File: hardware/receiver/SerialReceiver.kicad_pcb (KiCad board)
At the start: 2 copper layers, 78.7 x 70.5 mm, 30 parts, among them J1 DATA, J2 CONTROL, J3 RX, J4 Clock select, J5 Conn_01x03_Male, J6 Clock select, SW1 SW_Push, U1 74HC132, U2 74HC191, U3 74HC191, U4 74HC595, U5 74HC74, U6 74LS244

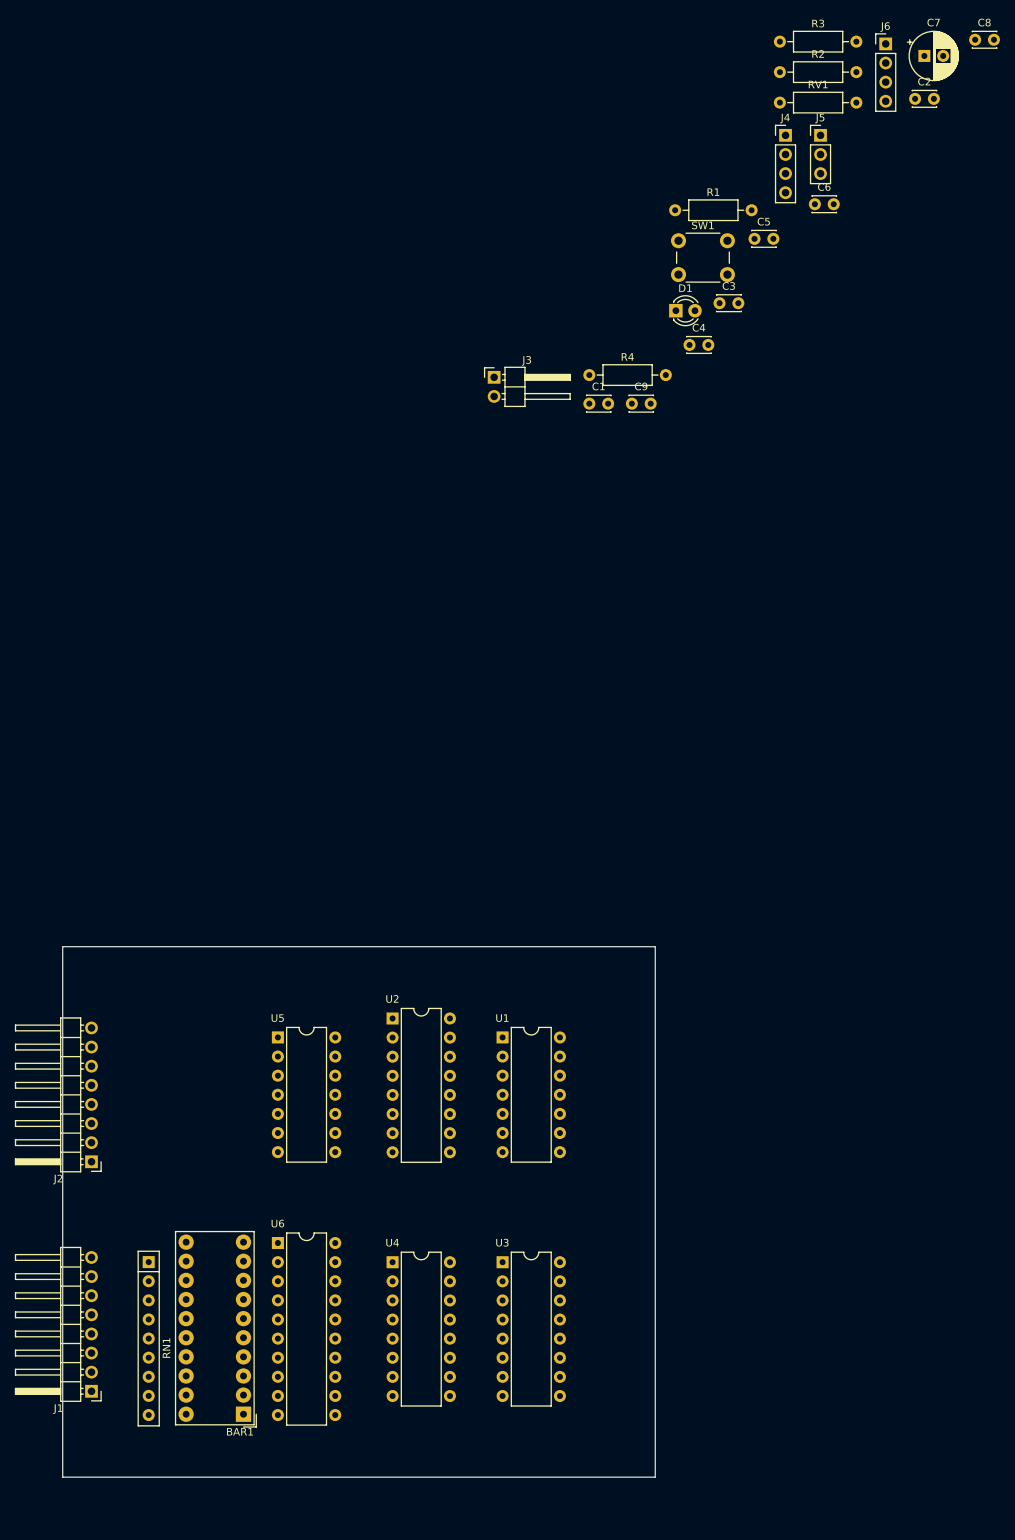
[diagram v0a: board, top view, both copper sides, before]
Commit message: Changed the layout of the schematic for better wiring.
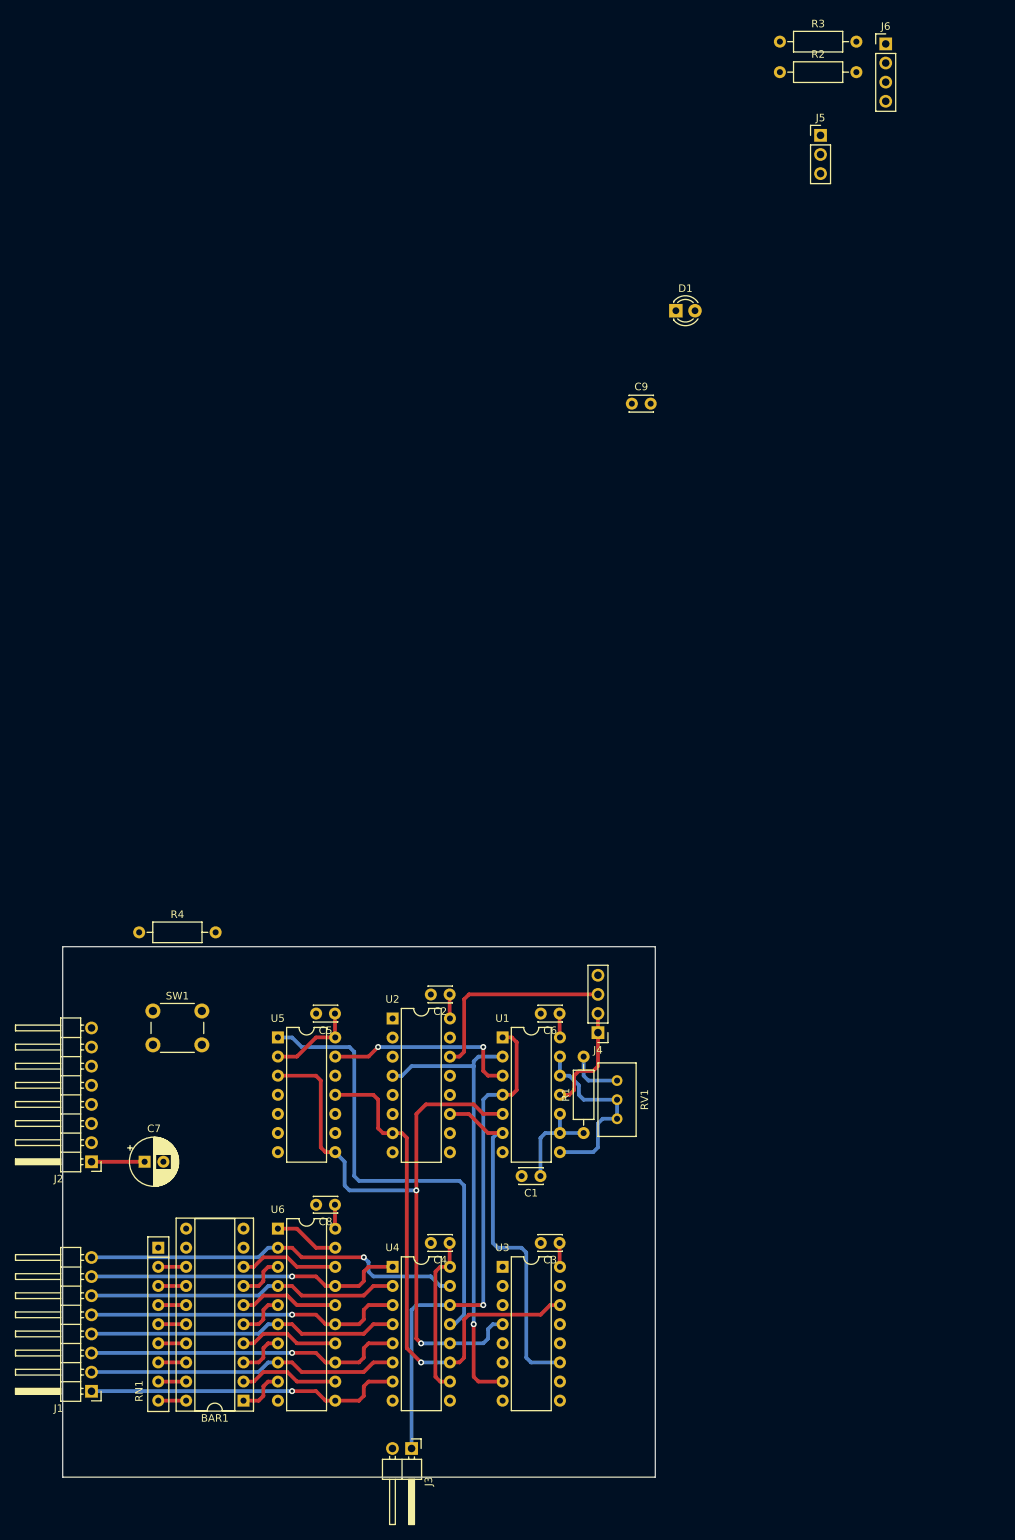
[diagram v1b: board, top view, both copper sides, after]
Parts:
- BAR1: footprint Display:HDSP-4830 -> Package_DIP:DIP-20_W7.62mm_Socket
- RV1: footprint Resistor_THT:R_Axial_DIN0207_L6.3mm_D2.5mm_P10.16mm_Horizontal -> Potentiometer_THT:Potentiometer_Bourns_3296W_Vertical
- moved C7 179.8 mm to (130.3, 90.8)
- moved C8 176.6 mm to (155.6, 96.5), turned to 180 degrees
- moved J3 142.7 mm to (165.7, 128.9), turned to -90 degrees
- moved RV1 136.7 mm to (193.0, 85.1), turned to -90 degrees
- moved C2 134.1 mm to (170.8, 68.6), turned to 180 degrees
- moved C3 126.7 mm to (185.4, 101.6), turned to 180 degrees
- moved SW1 123.9 mm to (131.4, 70.8)
- moved C4 123.5 mm to (170.8, 101.6), turned to 180 degrees
- moved R1 123.2 mm to (188.6, 87.0), turned to 90 degrees
- moved J4 121.8 mm to (190.5, 73.7), turned to 180 degrees
- moved C5 117.1 mm to (155.6, 71.1), turned to 180 degrees
- moved C6 112.8 mm to (185.4, 71.1), turned to 180 degrees
- moved C1 102.8 mm to (182.9, 92.7), turned to 180 degrees
- moved R4 95.2 mm to (129.5, 60.3)
- moved RN1 2.29 mm to (132.1, 102.2)
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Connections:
- BAR1 pad 1: Net-(BAR1-Pad1) -> /DO0
- BAR1 pad 2: Net-(BAR1-Pad2) -> /DO1
- BAR1 pad 3: Net-(BAR1-Pad3) -> /DO2
- BAR1 pad 4: Net-(BAR1-Pad4) -> /DO3
- BAR1 pad 5: Net-(BAR1-Pad5) -> /DO4
- BAR1 pad 6: Net-(BAR1-Pad6) -> /DO5
- BAR1 pad 7: Net-(BAR1-Pad7) -> /DO6
- BAR1 pad 8: Net-(BAR1-Pad8) -> /DO7
- RN1 pad 2: Net-(BAR1-Pad20) -> Net-(BAR1-Pad13)
- RN1 pad 3: Net-(BAR1-Pad19) -> Net-(BAR1-Pad14)
- RN1 pad 4: Net-(BAR1-Pad18) -> Net-(BAR1-Pad15)
- RN1 pad 5: Net-(BAR1-Pad17) -> Net-(BAR1-Pad16)
- RN1 pad 6: Net-(BAR1-Pad16) -> Net-(BAR1-Pad17)
- RN1 pad 7: Net-(BAR1-Pad15) -> Net-(BAR1-Pad18)
- RN1 pad 8: Net-(BAR1-Pad14) -> Net-(BAR1-Pad19)
- RN1 pad 9: Net-(BAR1-Pad13) -> Net-(BAR1-Pad20)
- U1 pad 1: Net-(C1-Pad1) -> Net-(J3-Pad1)
- U1 pad 10: Net-(U1-Pad10) -> Net-(C1-Pad1)
- U1 pad 11: Net-(U1-Pad11) -> Net-(J4-Pad1)
- U1 pad 12: Net-(J3-Pad1) -> Net-(RV1-Pad1)
- U1 pad 13: Net-(U1-Pad13) -> Net-(RV1-Pad1)
- U1 pad 2: Net-(C1-Pad1) -> Net-(U2-Pad4)
- U1 pad 3: Net-(RV1-Pad1) -> Net-(U5-Pad13)
- U1 pad 4: Net-(RV1-Pad1) -> Net-(J3-Pad1)
- U1 pad 5: Net-(RV1-Pad1) -> Net-(U3-Pad4)
- U1 pad 6: Net-(J4-Pad1) -> Net-(U2-Pad11)
- U1 pad 8: Net-(U1-Pad8) -> Net-(RV1-Pad1)
- U1 pad 9: Net-(J3-Pad1) -> Net-(C1-Pad1)
- U2 pad 11: Net-(U1-Pad8) -> Net-(U2-Pad11)
- U2 pad 4: Net-(U1-Pad13) -> Net-(U2-Pad4)
- U3 pad 11: Net-(U1-Pad8) -> Net-(U2-Pad11)
- U3 pad 4: Net-(U1-Pad10) -> Net-(U3-Pad4)
- U3 pad 7: Net-(U1-Pad13) -> Net-(U2-Pad4)
- U4 pad 1: /D1 -> /D6
- U4 pad 12: Net-(U1-Pad10) -> Net-(U3-Pad4)
- U4 pad 15: /D0 -> /D7
- U4 pad 2: /D2 -> /D5
- U4 pad 3: /D3 -> /D4
- U4 pad 4: /D4 -> /D3
- U4 pad 5: /D5 -> /D2
- U4 pad 6: /D6 -> /D1
- U4 pad 7: /D7 -> /D0
- U5 pad 1: Net-(U1-Pad11) -> Net-(J2-Pad4)
- U5 pad 11: Net-(U1-Pad10) -> Net-(U2-Pad7)
- U5 pad 13: Net-(J2-Pad4) -> Net-(U5-Pad13)
- U5 pad 3: Net-(U2-Pad7) -> Net-(U3-Pad4)
- U5 pad 5: unconnected-(U5-Pad5) -> Net-(J2-Pad7)
- U5 pad 6: Net-(U1-Pad10) -> Net-(D1-Pad1)
- U5 pad 8: Net-(D1-Pad1) -> Net-(U3-Pad4)
- U5 pad 9: Net-(J2-Pad7) -> unconnected-(U5-Pad9)
- U6 pad 11: /D7 -> /D0
- U6 pad 12: Net-(BAR1-Pad4) -> /DO1
- U6 pad 13: /D5 -> /D2
- U6 pad 14: Net-(BAR1-Pad3) -> /DO3
- U6 pad 15: /D3 -> /D4
- U6 pad 16: Net-(BAR1-Pad2) -> /DO5
- U6 pad 17: /D1 -> /D6
- U6 pad 18: Net-(BAR1-Pad1) -> /DO7
- U6 pad 2: /D0 -> /D7
- U6 pad 3: Net-(BAR1-Pad8) -> /DO6
- U6 pad 4: /D2 -> /D5
- U6 pad 5: Net-(BAR1-Pad7) -> /DO4
- U6 pad 6: /D4 -> /D3
- U6 pad 7: Net-(BAR1-Pad6) -> /DO2
- U6 pad 8: /D6 -> /D1
- U6 pad 9: Net-(BAR1-Pad5) -> /DO0
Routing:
- net Net-(U3-Pad4): track 0.00 -> 87.7 mm, vias 0 -> 2
- net Net-(U2-Pad7): track 0.00 -> 69.3 mm, vias 0 -> 1
- net Net-(J3-Pad1): track 0.00 -> 69.0 mm, vias 0 -> 1
- net Net-(J2-Pad4): track 0.00 -> 62.1 mm
- net Net-(U2-Pad4): track 0.00 -> 61.4 mm, vias 0 -> 1
- net VCC: track 0.00 -> 53.2 mm
- net /D7: track 0.00 -> 51.0 mm, vias 0 -> 1
- net Net-(U2-Pad11): track 0.00 -> 47.3 mm
- net /D0: track 0.00 -> 42.3 mm, vias 0 -> 1
- net /D6: track 0.00 -> 42.3 mm, vias 0 -> 1
- net /D4: track 0.00 -> 42.3 mm, vias 0 -> 1
- net /D2: track 0.00 -> 42.3 mm, vias 0 -> 1
- net /D3: track 0.00 -> 41.6 mm
- net /D1: track 0.00 -> 41.6 mm
- net /D5: track 0.00 -> 41.6 mm
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
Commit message: Made an RX input protection, and almost finished the PCB.
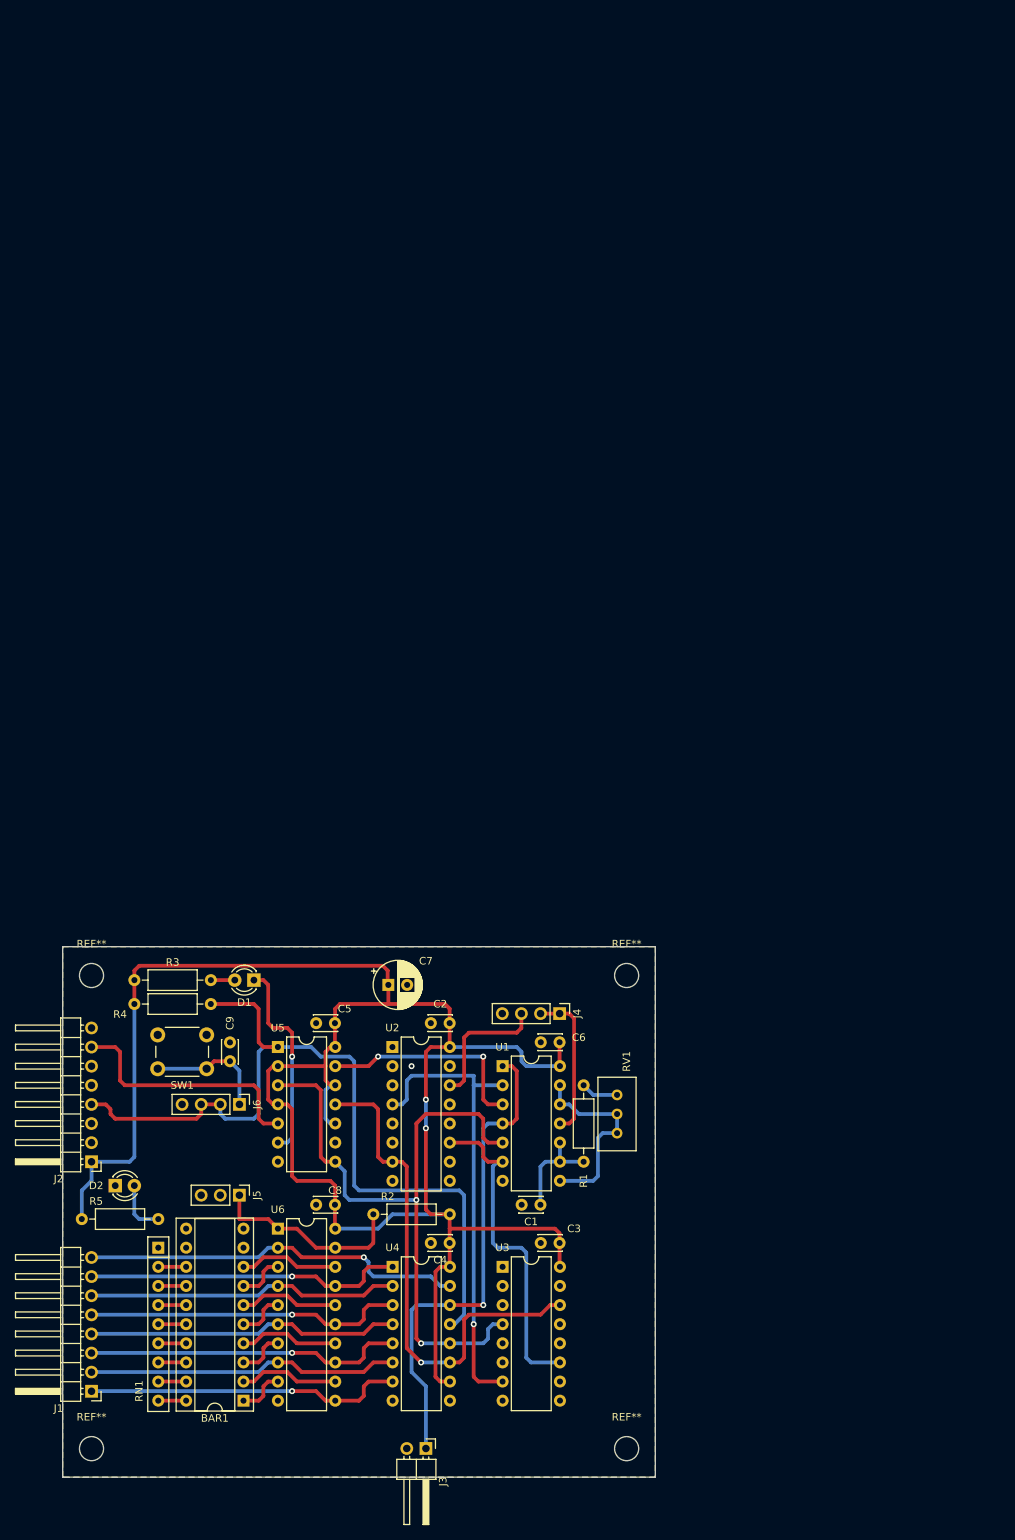
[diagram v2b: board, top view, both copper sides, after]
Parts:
- added D2: LED, LED_THT:LED_D3.0mm, F.Cu at (126.4, 94.0)
- added R5: 1k, Resistor_THT:R_Axial_DIN0207_L6.3mm_D2.5mm_P10.16mm_Horizontal, F.Cu at (121.9, 98.4)
- added REF**: MountingHole_3.2mm_M3, MountingHole:MountingHole_3.2mm_M3, F.Cu at (194.3, 66.1)
- added REF**: MountingHole_3.2mm_M3, MountingHole:MountingHole_3.2mm_M3, F.Cu at (123.2, 66.1)
- added REF**: MountingHole_3.2mm_M3, MountingHole:MountingHole_3.2mm_M3, F.Cu at (123.2, 128.9)
- added REF**: MountingHole_3.2mm_M3, MountingHole:MountingHole_3.2mm_M3, F.Cu at (194.3, 128.9)
- J5: value Conn_01x03_Male -> LED enable
- J6: value Clock select -> Mode select
- moved J6 165.0 mm to (142.9, 83.2), turned to -90 degrees
- moved R2 161.1 mm to (160.7, 97.8)
- moved J5 160.6 mm to (142.9, 95.2), turned to -90 degrees
- moved R3 151.3 mm to (128.9, 66.7)
- moved D1 105.1 mm to (144.8, 66.7), turned to 180 degrees
- moved C9 102.4 mm to (141.6, 77.5), turned to 90 degrees
- moved C7 40.0 mm to (162.6, 67.3)
- moved R4 13.5 mm to (139.1, 69.8), turned to 180 degrees
- moved J4 5.68 mm to (185.4, 71.1), turned to -90 degrees
- moved C1 3.81 mm to (182.9, 96.5)
- moved C2 3.81 mm to (170.8, 72.4)
- moved C6 3.81 mm to (185.4, 74.9)
- moved R1 3.81 mm to (188.6, 90.8)
- moved U1 3.81 mm to (177.8, 78.1)
- moved U2 3.80 mm to (163.2, 75.6)
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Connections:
- R4 pad 1: Net-(C9-Pad1) -> Net-(J2-Pad4)
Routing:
- net VCC: track 53.2 -> 261.8 mm, vias 0 -> 1
- net Net-(J2-Pad4): track 62.1 -> 112.5 mm
- net Net-(J2-Pad7): track 0.00 -> 33.4 mm
- net Net-(D1-Pad1): track 0.00 -> 27.1 mm, vias 0 -> 1
- net Net-(J5-Pad1): track 8.68 -> 26.6 mm
- net Net-(C9-Pad1): track 0.00 -> 16.3 mm
- net Net-(J4-Pad3): track 27.2 -> 17.9 mm
- net Net-(D2-Pad2): track 0.00 -> 7.25 mm
- net Net-(J4-Pad1): track 14.7 -> 20.2 mm
- net Net-(D1-Pad2): track 0.00 -> 3.18 mm
- net Net-(U1-Pad6): track 47.3 -> 44.2 mm
- net Net-(J3-Pad1): track 69.0 -> 66.0 mm
- net Net-(U1-Pad3): track 26.2 -> 28.7 mm
- net Net-(R1-Pad2): track 7.25 -> 4.98 mm
- net Net-(U2-Pad7): track 69.3 -> 68.1 mm
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- added copper zone on B.Cu, net GND
- added copper zone on F.Cu, net GND
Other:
- board text added: "!RD"
- board text added: "ALWAYS"
- board text added: "BUTTON"
- board text added: "D0"
- board text added: "D1"
- board text added: "D2"
- board text added: "D3"
- board text added: "D4"
- board text added: "D5"
- board text added: "D6"
- board text added: "D7"
- board text added: "EXT. CLOCK"
- board text added: "GND"
- board text added: "MANUAL"
- board text added: "ON"
- board text added: "READY"
- board text added: "Ready"
- board text added: "VCC"

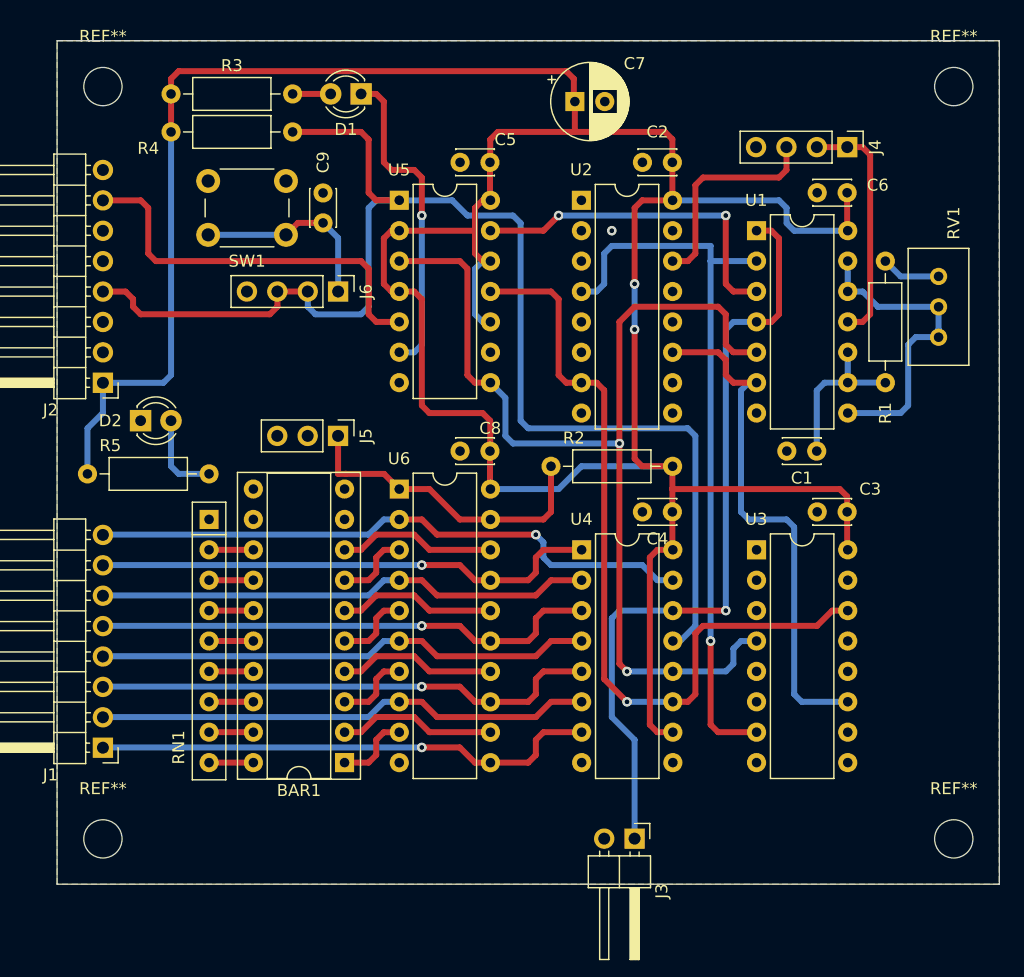
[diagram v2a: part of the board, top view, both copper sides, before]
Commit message: Input protection is now on the PCB.
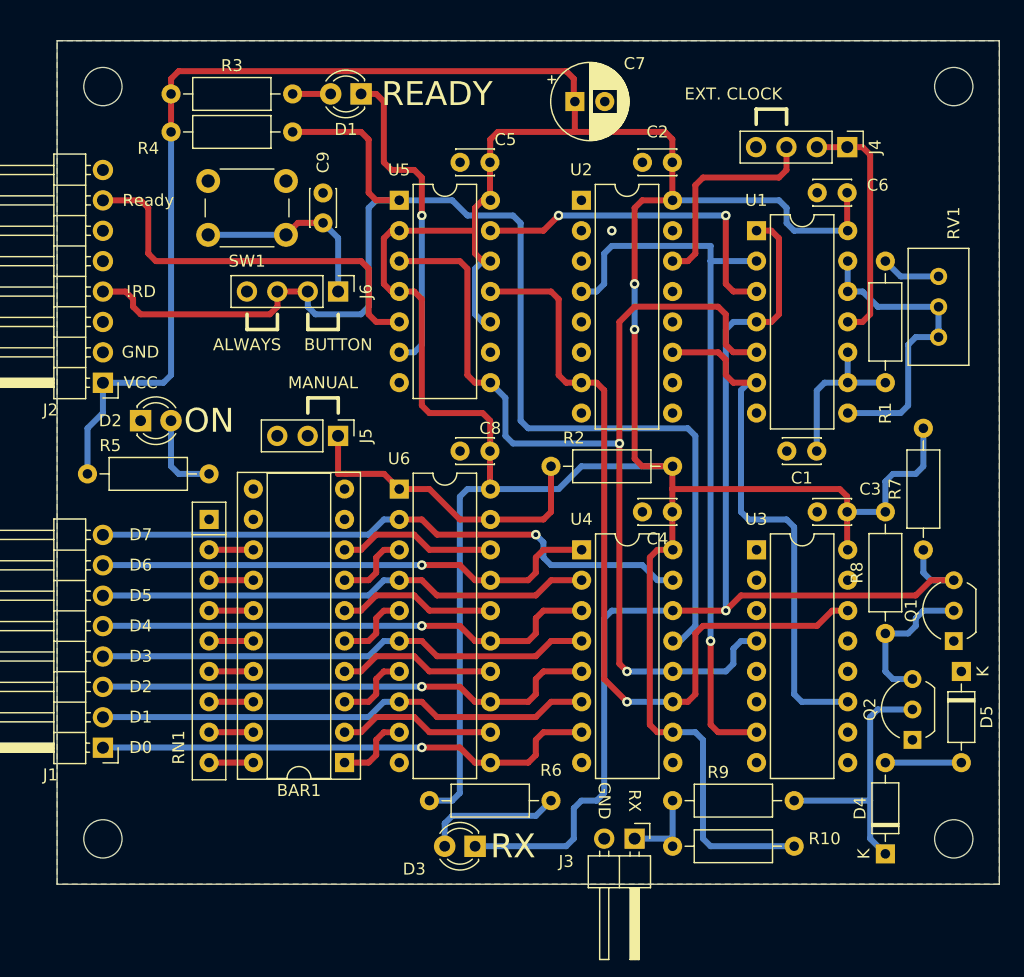
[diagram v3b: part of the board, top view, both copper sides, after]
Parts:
- added D3: LED, LED_THT:LED_D3.0mm, F.Cu at (154.3, 129.5)
- added D4: D_Zener, Diode_THT:D_DO-35_SOD27_P7.62mm_Horizontal, F.Cu at (188.6, 130.2)
- added D5: D_Zener, Diode_THT:D_DO-35_SOD27_P7.62mm_Horizontal, F.Cu at (194.9, 114.9)
- added Q1: 2N7000, Package_TO_SOT_THT:TO-92_Inline_Wide, F.Cu at (194.3, 112.4)
- added Q2: 2N7000, Package_TO_SOT_THT:TO-92_Inline_Wide, F.Cu at (190.9, 120.7)
- added R10: 20k, Resistor_THT:R_Axial_DIN0207_L6.3mm_D2.5mm_P10.16mm_Horizontal, F.Cu at (170.8, 129.5)
- added R6: 1k, Resistor_THT:R_Axial_DIN0207_L6.3mm_D2.5mm_P10.16mm_Horizontal, F.Cu at (150.5, 125.7)
- added R7: 10k, Resistor_THT:R_Axial_DIN0207_L6.3mm_D2.5mm_P10.16mm_Horizontal, F.Cu at (191.8, 104.8)
- added R8: 4k7, Resistor_THT:R_Axial_DIN0207_L6.3mm_D2.5mm_P10.16mm_Horizontal, F.Cu at (188.6, 111.8)
- added R9: 510, Resistor_THT:R_Axial_DIN0207_L6.3mm_D2.5mm_P10.16mm_Horizontal, F.Cu at (170.8, 125.7)
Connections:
- U1 pad 1: Net-(J3-Pad1) -> Net-(U1-Pad1)
- U1 pad 4: Net-(J3-Pad1) -> Net-(U1-Pad1)
- U4 pad 14: Net-(J3-Pad1) -> Net-(U1-Pad1)
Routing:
- net Net-(U1-Pad1): track 0.00 -> 100.9 mm, vias 0 -> 1
- net VCC: track 261.8 -> 323.7 mm
- net Net-(J3-Pad1): track 66.0 -> 6.98 mm, vias 1 -> 0
- net Net-(D4-Pad1): track 0.00 -> 22.1 mm
- net Net-(Q1-Pad2): track 0.00 -> 12.6 mm
- net Net-(D3-Pad2): track 0.00 -> 11.6 mm
- net Net-(D4-Pad2): track 0.00 -> 6.35 mm
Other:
- board text added: "RX"
